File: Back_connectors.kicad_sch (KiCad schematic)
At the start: 3 parts

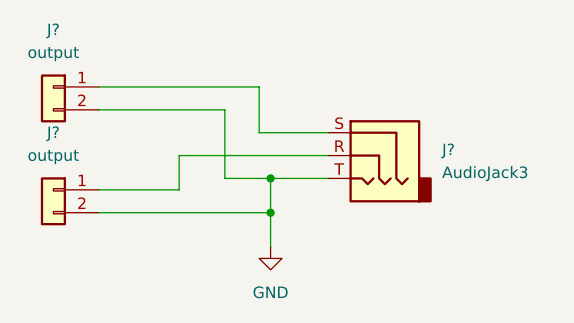
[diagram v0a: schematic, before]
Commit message: New power supply
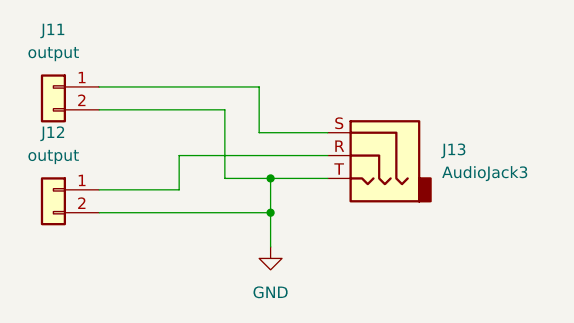
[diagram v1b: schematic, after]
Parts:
- gave numbers to parts that had none: 3
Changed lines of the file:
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@@
   (symbol (lib_id "power:GND") (at 85.09 53.34 0) (unit 1)
     (in_bom yes) (on_board yes) (fields_autoplaced)
-    (property "Reference" "#PWR?" (id 0) (at 85.09 59.69 0)
+    (property "Reference" "#PWR027" (id 0) (at 85.09 59.69 0)
       (effects (font (size 1.27 1.27)) hide)
     )
@@
   (symbol (lib_id "Connector:AudioJack3") (at 96.52 43.18 0) (mirror y) (unit 1)
     (in_bom yes) (on_board yes) (fields_autoplaced)
-    (property "Reference" "J?" (id 0) (at 104.14 42.5449 0)
+    (property "Reference" "J13" (id 0) (at 104.14 42.5449 0)
       (effects (font (size 1.27 1.27)) (justify right))
     )
@@
   (symbol (lib_id "Connector_Generic:Conn_01x02") (at 60.96 35.56 0) (mirror y) (unit 1)
     (in_bom yes) (on_board yes) (fields_autoplaced)
-    (property "Reference" "J?" (id 0) (at 60.96 29.21 0))
+    (property "Reference" "J11" (id 0) (at 60.96 29.21 0))
     (property "Value" "output" (id 1) (at 60.96 31.75 0))
     (property "Footprint" "spdf1626_lib:PinHeader_1x02_P2.54mm" (id 2) (at 60.96 35.56 0)
@@
   (symbol (lib_id "Connector_Generic:Conn_01x02") (at 60.96 46.99 0) (mirror y) (unit 1)
     (in_bom yes) (on_board yes) (fields_autoplaced)
-    (property "Reference" "J?" (id 0) (at 60.96 40.64 0))
+    (property "Reference" "J12" (id 0) (at 60.96 40.64 0))
     (property "Value" "output" (id 1) (at 60.96 43.18 0))
     (property "Footprint" "spdf1626_lib:PinHeader_1x02_P2.54mm" (id 2) (at 60.96 46.99 0)
